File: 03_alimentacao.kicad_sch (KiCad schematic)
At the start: 29 parts, among them T3 TP_DGND, T4 TP_+5V_REG, T5 TP_+3.3V_DIG, T6 TP_+3.3V_ANA, U1 R-78HB5.0-0.5L, U2 MCP1824ST-3302E/DB, U3 SPX3819M5-L-3-3/TR, U4 TL431B

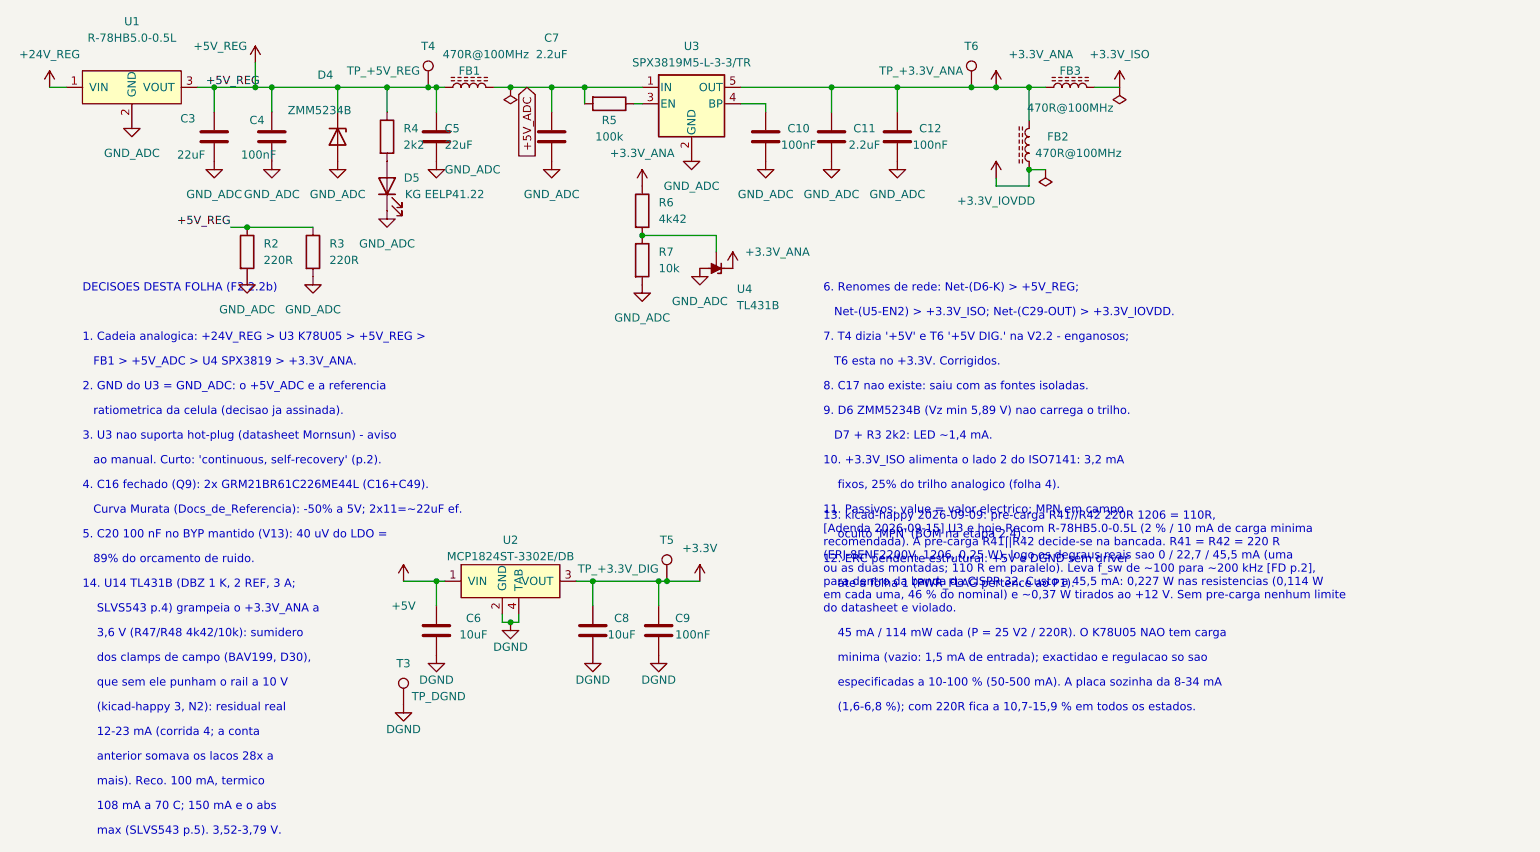
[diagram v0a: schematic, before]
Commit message: Esquematico: alimentacao do lado PLC passa da folha 3 para a folha 4
U2 (MCP1824, +3.3V do lado DGND), C6, C8, C9, T3 e T5 desenhados na
folha 4 (barreira digital), junto ao ISO7141 que alimentam. Limpeza
grafica nas folhas 2 e 6 (rectangulos e fios soltos).

Sem mudanca electrica: netlist com os mesmos 148 componentes e nenhum
pino com rede diferente; ERC 0 erros; DRC 0 erros, paridade 0.

Co-Authored-By: Claude Opus 5.5 (1M context) <noreply@anthropic.com>
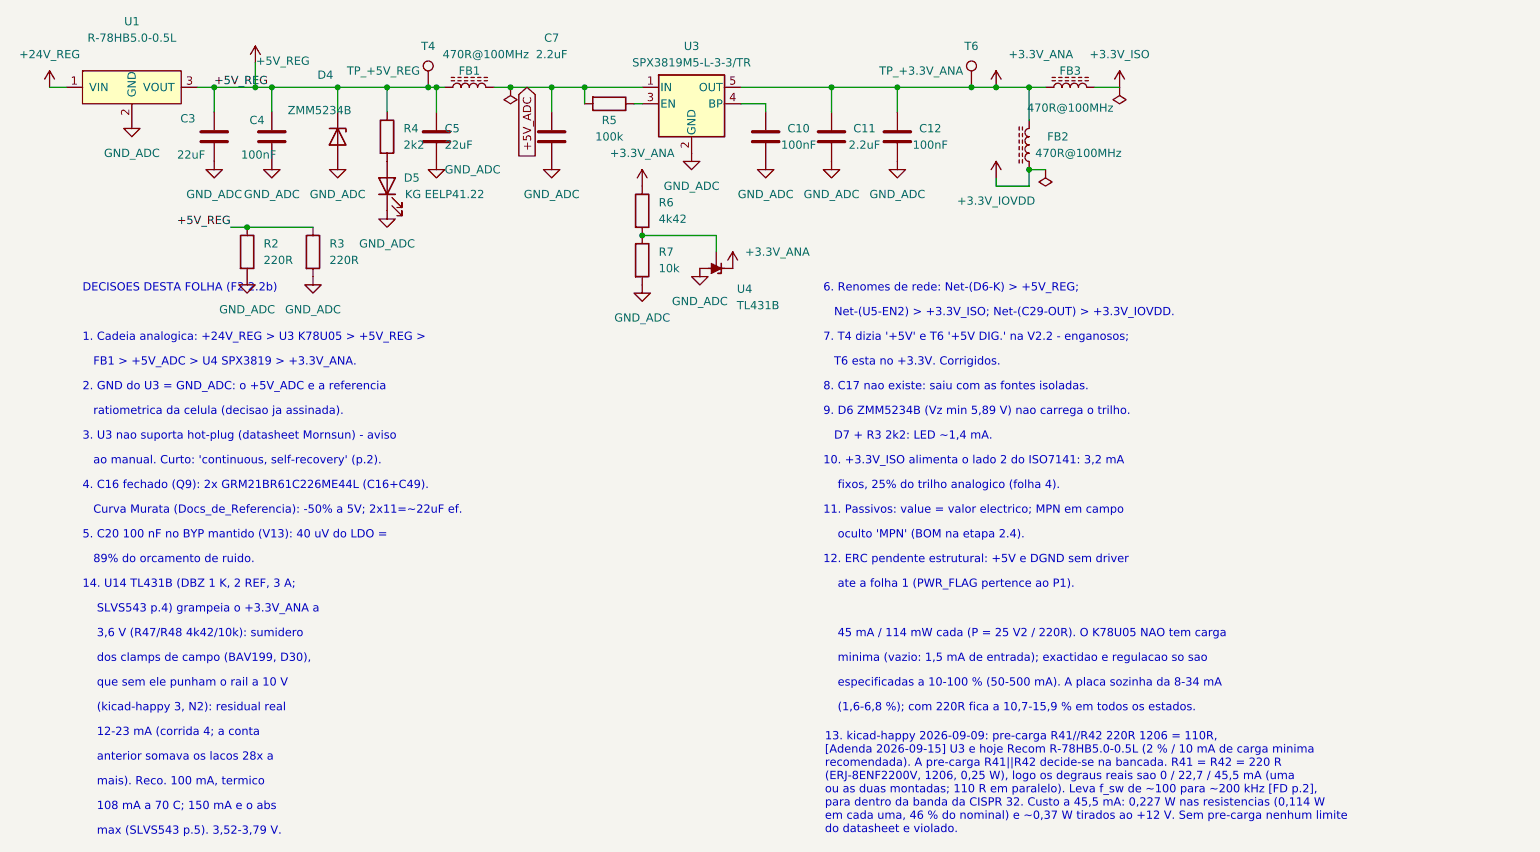
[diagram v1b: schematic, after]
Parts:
- removed C6, C8: 10uF, EBM7_V23:0603C, symbol Device:C
- removed C9: 100nF, EBM7_V23:0603C, symbol Device:C
- removed T3: TP_DGND, EBM7_V23:TestPad_Via, symbol Connector:TestPoint
- removed T5: TP_+3.3V_DIG, EBM7_V23:TestPad_Via, symbol Connector:TestPoint
- removed U2: MCP1824ST-3302E/DB, EBM7_V23:SOT-223-3, symbol EBM7_V23_proyecto2:MCP1824ST-3302E
